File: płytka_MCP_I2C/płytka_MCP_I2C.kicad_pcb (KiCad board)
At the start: 2 copper layers, 98 x 92 mm, 32 parts, among them J1 A0, J10 V0, J11 Ext, J12 I2C, J14 U1, J15 U2, J16 U3, J17 RS, J18 K, J19 A, J2 A1, J20 VDD, J21 GND, J23 VSS, J24 Conn_01x16_Pin, J25 LCD, J26 VCC, J3 A2, J4 SDA, J5 SCL, J6 INTA, J7 INTB, J8 INTA, U1 MCP23017_SP

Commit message: MCP I2C wersja 1.0
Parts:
- moved J20 76.9 mm to (91.8, 90.8)
- moved J26 66.3 mm to (98.5, 88.7), turned to 0 degrees
- moved J12 63.9 mm to (107.9, 80.5)
- moved J23 61.9 mm to (84.0, 90.8)
- moved J21 51.2 mm to (105.0, 88.8), turned to 0 degrees
- moved C1 49.4 mm to (89.7, 80.4), turned to 90 degrees
- moved J1 29.5 mm to (90.7, 49.5)
- moved J2 29.5 mm to (85.7, 49.5)
- moved J3 29.5 mm to (80.7, 49.5)
- moved J19 23.2 mm to (52.1, 59.0)
- moved R1 18.4 mm to (98.2, 46.3), turned to -90 degrees
- moved J8 14.6 mm to (73.2, 53.6), turned to 180 degrees
- moved J18 7.02 mm to (52.1, 53.2)
- moved R2 5.16 mm to (109.4, 46.3)
- moved R3 5.07 mm to (115.1, 46.3)
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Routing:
- net VCC: track 0.00 -> 195.8 mm
- net Net-(J18-Pin_1): track 0.00 -> 135.7 mm
- net Net-(J19-Pin_1): track 0.00 -> 132.4 mm
- net GND: track 0.00 -> 121.3 mm
- net Net-(J10-Pin_2): track 0.00 -> 83.9 mm
- net Net-(J16-Pin_8): track 0.00 -> 72.8 mm
- net Net-(J17-Pin_1): track 0.00 -> 68.9 mm
- net Net-(J16-Pin_7): track 0.00 -> 67.4 mm
- net Net-(J17-Pin_2): track 0.00 -> 66.3 mm
- net Net-(J17-Pin_3): track 0.00 -> 64.9 mm
- net Net-(J16-Pin_6): track 0.00 -> 62.4 mm
- net Net-(J20-Pin_1): track 0.00 -> 62.0 mm
- net Net-(J16-Pin_5): track 0.00 -> 56.9 mm
- net Net-(J23-Pin_1): track 0.00 -> 54.6 mm
- net Net-(J16-Pin_4): track 0.00 -> 51.2 mm
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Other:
- board size 98 x 92 mm -> 98 x 77 mm

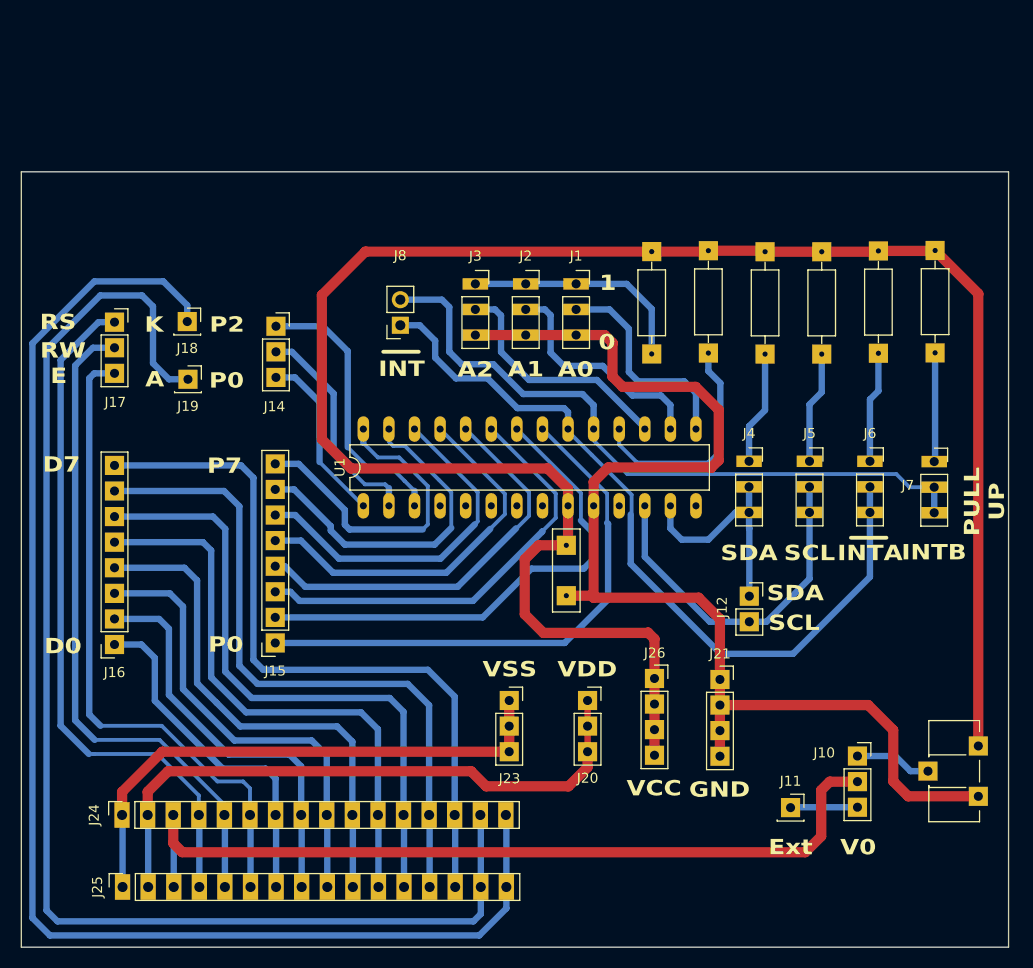
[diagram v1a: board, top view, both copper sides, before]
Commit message: Kosmetyczne zmiany, wydruk schematu, oraz plytki do pdf
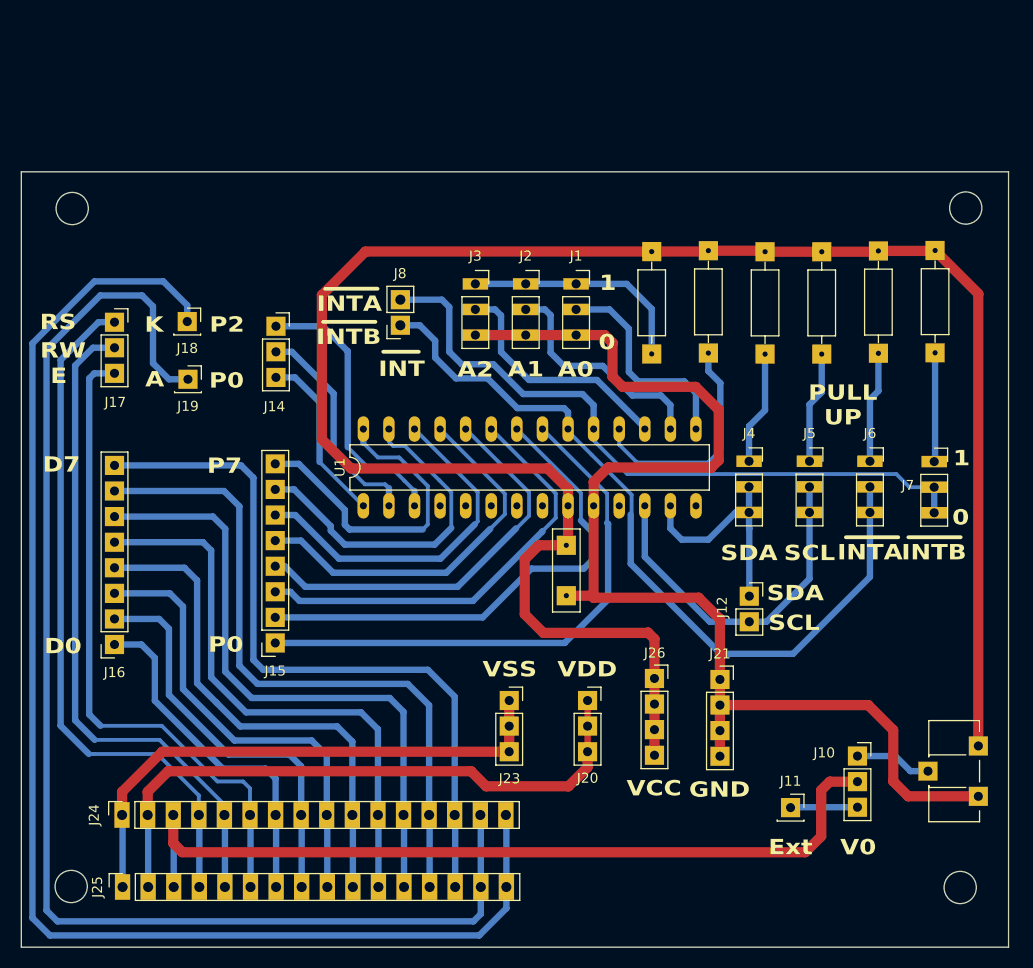
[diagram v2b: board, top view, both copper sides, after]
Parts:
- added ?: , , F.Cu at (40.6, 42.0)
- added ?: , , F.Cu at (40.5, 109.3)
- added ?: , , F.Cu at (128.8, 109.4)
- added ?: , , F.Cu at (129.3, 42.0)
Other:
- board text added: "INTA"
- board text added: "INTB"

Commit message: Dodany pin RESET
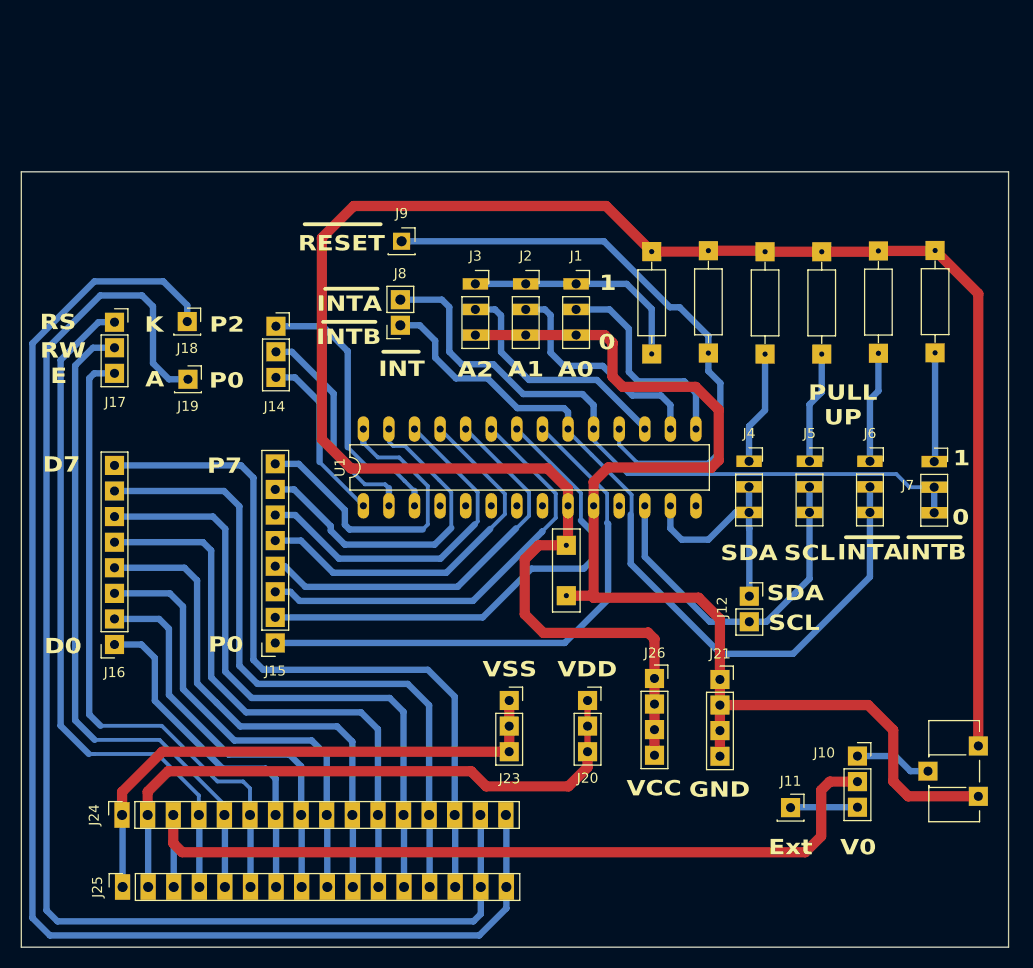
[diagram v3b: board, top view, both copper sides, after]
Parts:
- removed ? (x4): , 
- added J9: RESET, Connector_PinSocket_2.54mm:PinSocket_1x01_P2.54mm_Vertical, F.Cu at (73.3, 45.2)
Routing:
- net Net-(J9-Pin_1): track 23.0 -> 59.0 mm
- net VCC: track 195.8 -> 202.9 mm
